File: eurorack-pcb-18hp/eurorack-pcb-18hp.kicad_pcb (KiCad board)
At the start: 2 copper layers, 38.8 x 108.3 mm, 0 parts

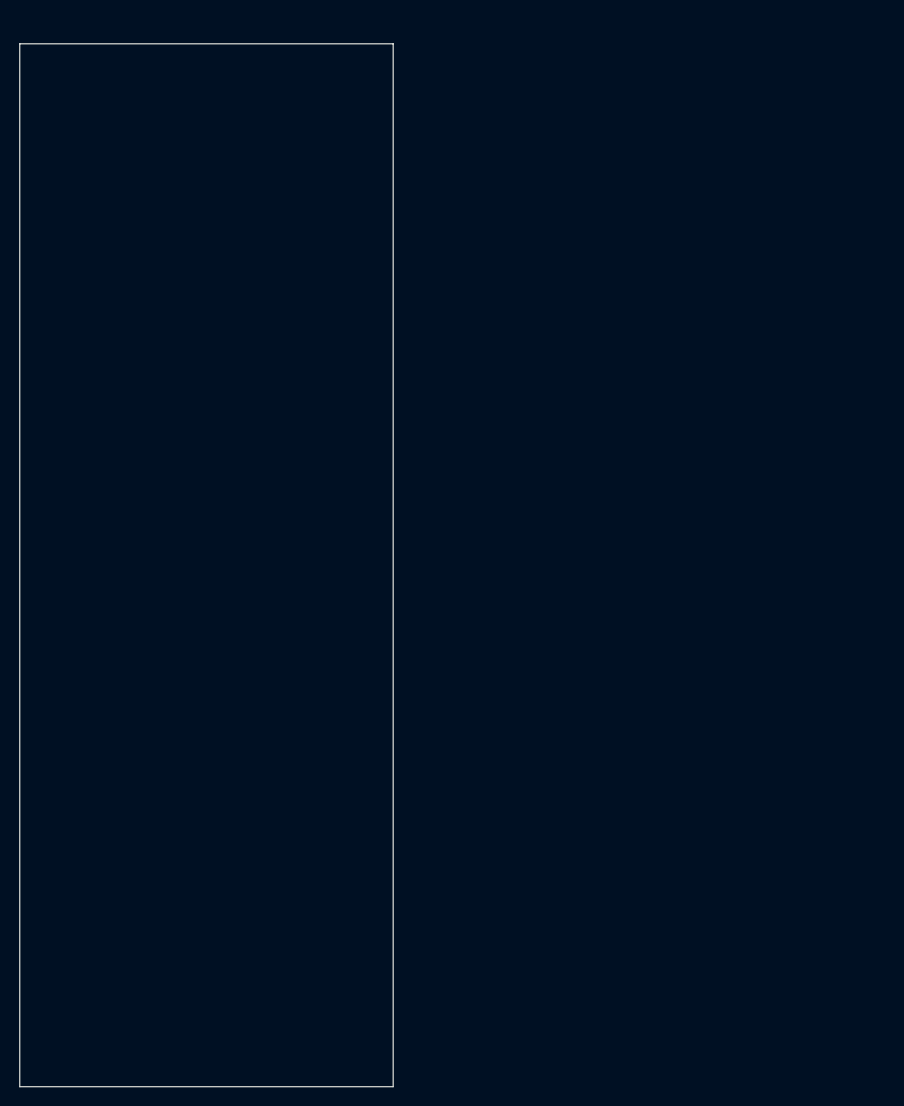
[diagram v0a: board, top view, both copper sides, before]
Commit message: Minor adjustments to PCB positioning. Moving everything into a single folder to be easier for kiCad to pick up all templates from user-template path
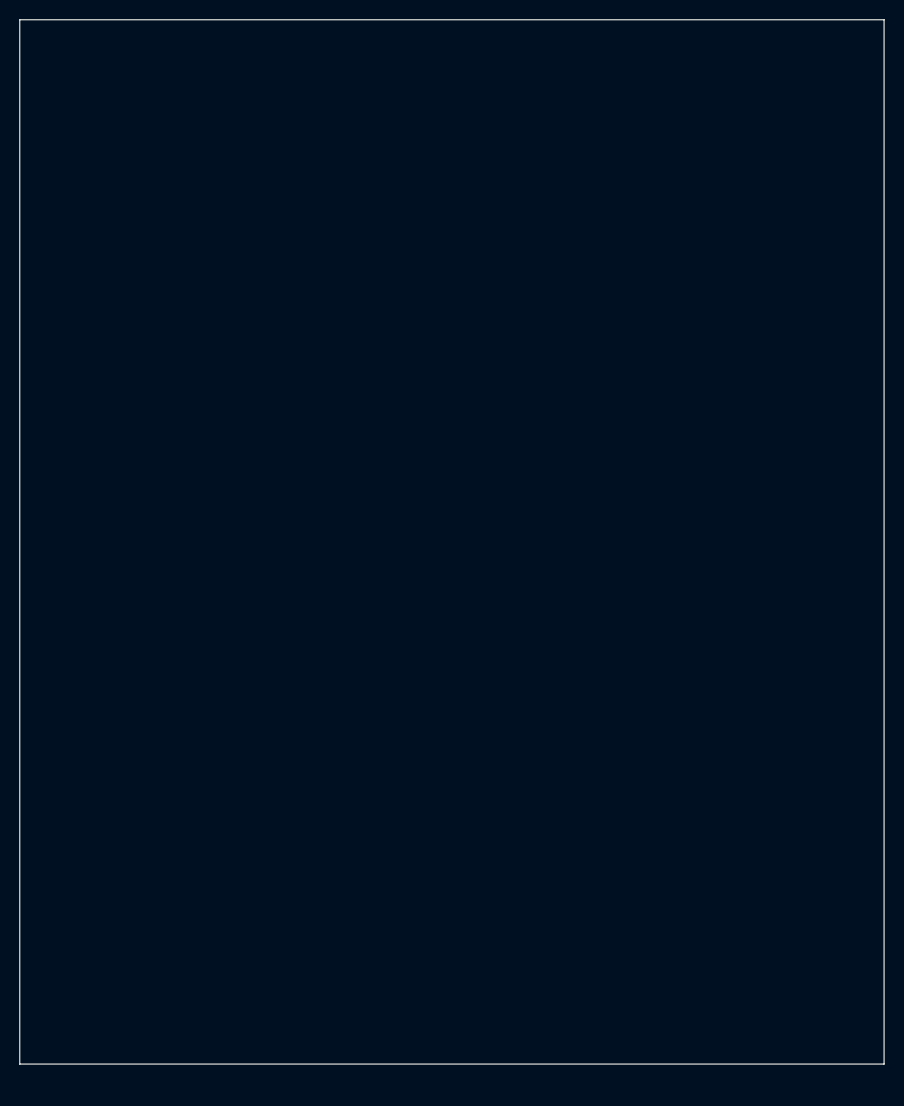
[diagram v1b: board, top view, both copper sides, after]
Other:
- board size 38.8 x 108.3 mm -> 89.8 x 108.5 mm
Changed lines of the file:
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@@
   )
   (net 0 "")
-  (gr_line (start 0.75 12.5) (end 0.75 120.85) (layer "Edge.Cuts") (width 0.1))
-  (gr_line (start 39.55 120.85) (end 39.55 12.5) (layer "Edge.Cuts") (width 0.1))
-  (gr_line (start 0.75 120.85) (end 39.55 120.85) (layer "Edge.Cuts") (width 0.1))
-  (gr_line (start 0.75 12.5) (end 39.55 12.5) (layer "Edge.Cuts") (width 0.1))
-  (gr_line (start 40.3 0) (end 40.3 128.5) (layer "User.1") (width 0.1))
+  (gr_line (start 0.75 10) (end 0.75 118.5) (layer "Edge.Cuts") (width 0.1))
+  (gr_line (start 90.55 118.5) (end 90.55 10) (layer "Edge.Cuts") (width 0.1))
+  (gr_line (start 0.75 118.5) (end 90.55 118.5) (layer "Edge.Cuts") (width 0.1))
+  (gr_line (start 0.75 10) (end 90.55 10) (layer "Edge.Cuts") (width 0.1))
+  (gr_line (start 91.3 0) (end 91.3 128.5) (layer "User.1") (width 0.1))
   (gr_line (start 0 128.5) (end 0 0) (layer "User.1") (width 0.1))
-  (gr_line (start 0 0) (end 40.3 0) (layer "User.1") (width 0.1))
-  (gr_line (start 40.3 128.5) (end 0 128.5) (layer "User.1") (width 0.1))
+  (gr_line (start 0 0) (end 91.3 0) (layer "User.1") (width 0.1))
+  (gr_line (start 91.3 128.5) (end 0 128.5) (layer "User.1") (width 0.1))
 )
